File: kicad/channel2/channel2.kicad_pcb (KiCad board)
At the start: 2 copper layers, 47.5 x 47.4 mm, 43 parts, among them J1 Conn_01x07_Male, J5V1 Conn_01x01_Male, Q1 BC846B, Q2 IRF3205, Q3 IRF3205, Q4 BC846B, Q5 IRF3205, Q6 IRF3205, U1 LM324

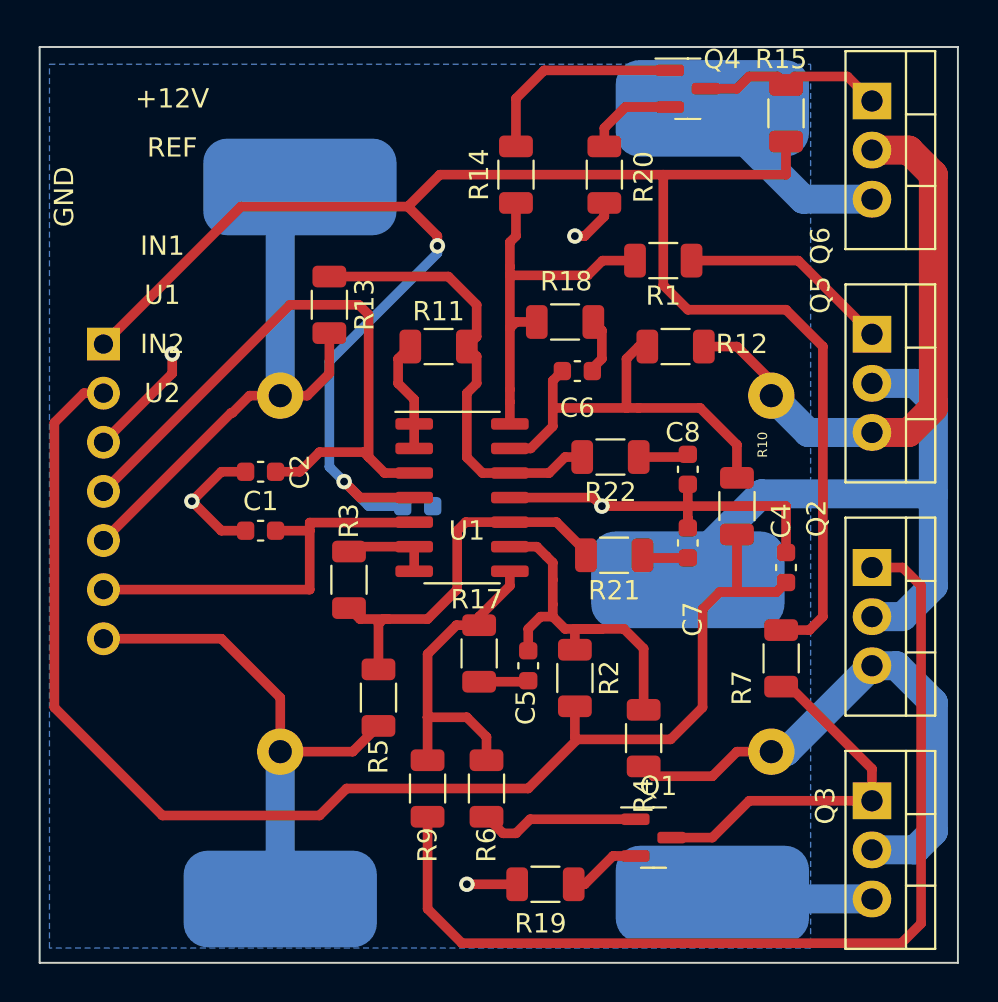
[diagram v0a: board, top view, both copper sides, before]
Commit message: work on pulse charge/discharge, combined board
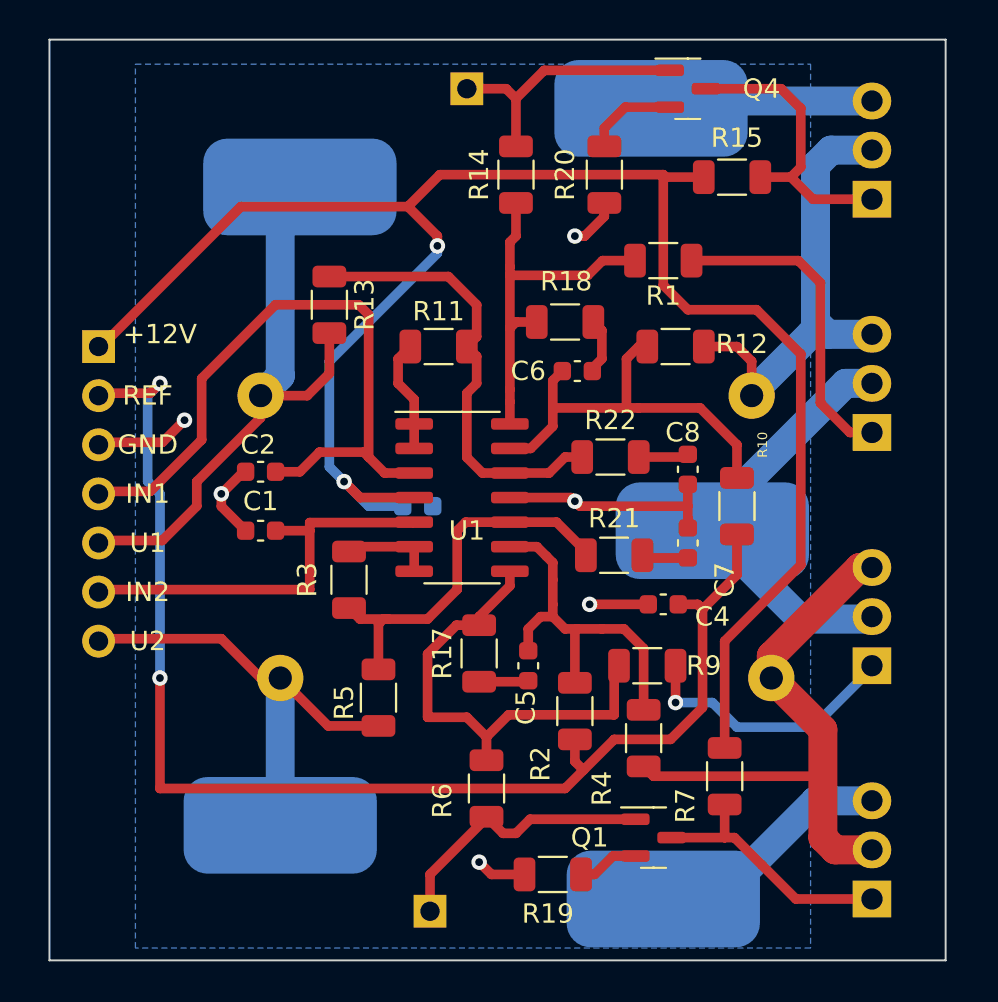
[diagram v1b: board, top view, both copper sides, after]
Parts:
- added JTest1: Conn_01x01_Male, Connector_PinHeader_2.54mm:PinHeader_1x01_P2.54mm_Vertical, B.Cu at (160.0, 73.7)
- added JTest2: Conn_01x01_Male, Connector_PinHeader_2.54mm:PinHeader_1x01_P2.54mm_Vertical, B.Cu at (158.1, 116.2)
- Q2, Q3, Q5, Q6: moved to B.Cu
- moved R9 13.0 mm to (169.4, 103.5), turned to 180 degrees
- moved R7 6.76 mm to (173.4, 109.2)
- moved C4 6.63 mm to (170.2, 100.3), turned to 180 degrees
- moved Q2 5.08 mm to (181.0, 103.5), turned to 90 degrees
- moved Q3 5.08 mm to (181.0, 115.6), turned to 90 degrees
- moved Q5 5.08 mm to (181.0, 91.4), turned to 90 degrees
- moved Q6 5.08 mm to (181.0, 79.4), turned to 90 degrees
- moved R15 4.33 mm to (173.7, 78.2), turned to 180 degrees
- moved R8 3.81 mm to (175.8, 104.1)
- moved JBat2 3.81 mm to (150.4, 111.8)
- moved JGND1 3.18 mm to (169.5, 74.7)
- moved J5V1 2.84 mm to (172.7, 96.5)
- moved JGND2 2.55 mm to (170.2, 115.6)
- moved R2 1.71 mm to (165.6, 105.9)
- moved R16 1.02 mm to (174.8, 89.5)
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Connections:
- net Net-(Q3-Pad3) renamed GND2
- net Net-(Q6-Pad3) renamed GND1
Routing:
- net Net-(Q2-Pad1): track 51.8 -> 14.0 mm, vias 0 -> 1
- net +5V: track 31.8 -> 22.0 mm
- net GND: track 37.9 -> 29.4 mm, vias 5 -> 6
- net Net-(R17-Pad1): track 16.9 -> 24.4 mm
- net Net-(Q5-Pad3): track 30.5 -> 23.8 mm
- net Net-(JTest2-Pad1): track 8.36 -> 14.5 mm
- net Net-(Q1-Pad3): track 19.3 -> 13.4 mm
- net Net-(Q5-Pad1): track 10.9 -> 16.7 mm
- net Net-(Q4-Pad3): track 9.74 -> 15.3 mm
- net GND2: track 8.36 -> 12.9 mm
- net ref: track 70.8 -> 67.2 mm, vias 0 -> 2
- net Net-(JTest1-Pad1): track 11.0 -> 13.8 mm
- net U2: track 26.5 -> 23.7 mm
- net IN1: track 33.3 -> 35.2 mm
- net U1: track 28.6 -> 30.4 mm
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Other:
- board size 47.5 x 47.4 mm -> 46.4 x 47.6 mm

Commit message: minor schematic cleanups, improve opamp compensation
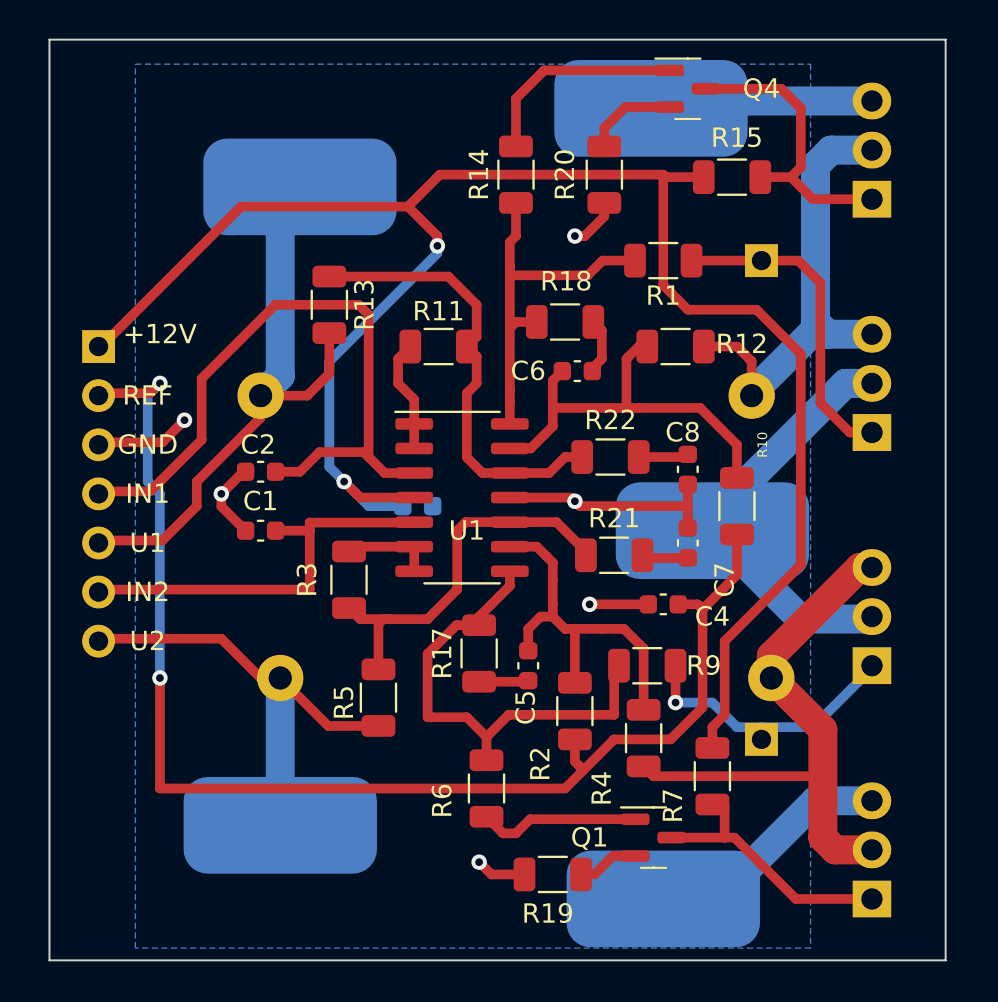
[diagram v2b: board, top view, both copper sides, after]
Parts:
- R14, R15, R6, R7: value 10k -> 22k
- R17, R18, R21, R22: value 22k -> 1k
- R19, R20: value 2.2k -> 1k
- moved JTest2 19.3 mm to (175.3, 107.3)
- moved JTest1 17.6 mm to (175.3, 82.5)
- moved R7 0.63 mm to (172.7, 109.2)
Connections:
- Q1 pad 1: Net-(JTest2-Pad1) -> Net-(Q1-Pad1)
- Q2 pad 1: Net-(Q2-Pad1) -> Net-(JTest2-Pad1)
- Q4 pad 1: Net-(JTest1-Pad1) -> Net-(Q4-Pad1)
- Q5 pad 1: Net-(Q5-Pad1) -> Net-(JTest1-Pad1)
- R1 pad 1: Net-(Q5-Pad1) -> Net-(JTest1-Pad1)
- R14 pad 1: Net-(JTest1-Pad1) -> Net-(Q4-Pad1)
- R6 pad 1: Net-(JTest2-Pad1) -> Net-(Q1-Pad1)
- R9 pad 1: Net-(Q2-Pad1) -> Net-(JTest2-Pad1)
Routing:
- net Net-(Q5-Pad1): track 16.7 -> 0.00 mm
- net Net-(Q2-Pad1): track 14.0 -> 0.00 mm, vias 1 -> 0
- net Net-(Q4-Pad1): track 0.00 -> 11.0 mm
- net Net-(Q1-Pad1): track 0.00 -> 8.36 mm
- net Net-(JTest1-Pad1): track 13.8 -> 16.7 mm
- net Net-(JTest2-Pad1): track 14.5 -> 14.6 mm, vias 0 -> 1
